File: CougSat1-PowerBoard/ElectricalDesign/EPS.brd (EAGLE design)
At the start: 90.4 x 95.8 mm, 414 parts, among them J1 Deployable 0, J11 CougSat Card, J2 PV1, J3 PV2, J5 SWD, J6 Umbilical, J7 PV0, J8 PV3, J9 Deployable 1, Q1 DMN53D0LDW, Q2 CSD25402Q3A, Q3 CSD25402Q3A, Q37 CSD25402Q3A, Q4 DMN2008LFU, Q5 CSD25402Q3A, Q6 DMN53D0LDW, Q8 DMN2008LFU, SW1 ESE24MH1, U1 TPS64200, U10 AD7689, U11 STM32L476RGT, U12 AD7689, U13 AD7291, U14 AD7291, U15 AD8515, U16 TPS64200, U17 AD8515, U18 INA199C1, U19 INA199C1, U2 AD7291, U20 BQ29700, U21 INA199C2, U22 INA199C1, U23 INA199C1, U24 INA199C1, U25 INA199C1, U26 TPS2115A, U27 TPS2115A, U28 TPS2115A, U29 TPS2115A, U3 AD7689, U30 TPS2115A, U31 TPS2115A, U32 TPS2115A, U33 TPS2115A, U34 TPS2115A, U35 TPS2115A, U36 TPS2115A, U37 TPS2115A, U38 TPS2115A, U39 TPS2115A, U4 TXS0102DQM, U40 TPS2115A, U41 TPS2115A, U42 TPS2115A, U43 TPS2115A, U44 TPS2115A, U45 TPS2115A, U46 TPS2115A, U47 TPS2115A, U48 TPS2115A, U49 TPS2115A, U5 TXS0102DQM, U50 TPS2115A, U51 AD8515, U52 TPS2115A, U53 TXS0102DQM, U54 TXS0102DQM, U55 TXS0102DQM, U6 BQ29700, U7 AD7291, U8 INA199C2, U9 AD7291, Y1 32.768kHz ±10ppm, Y2 8MHz ±10ppm

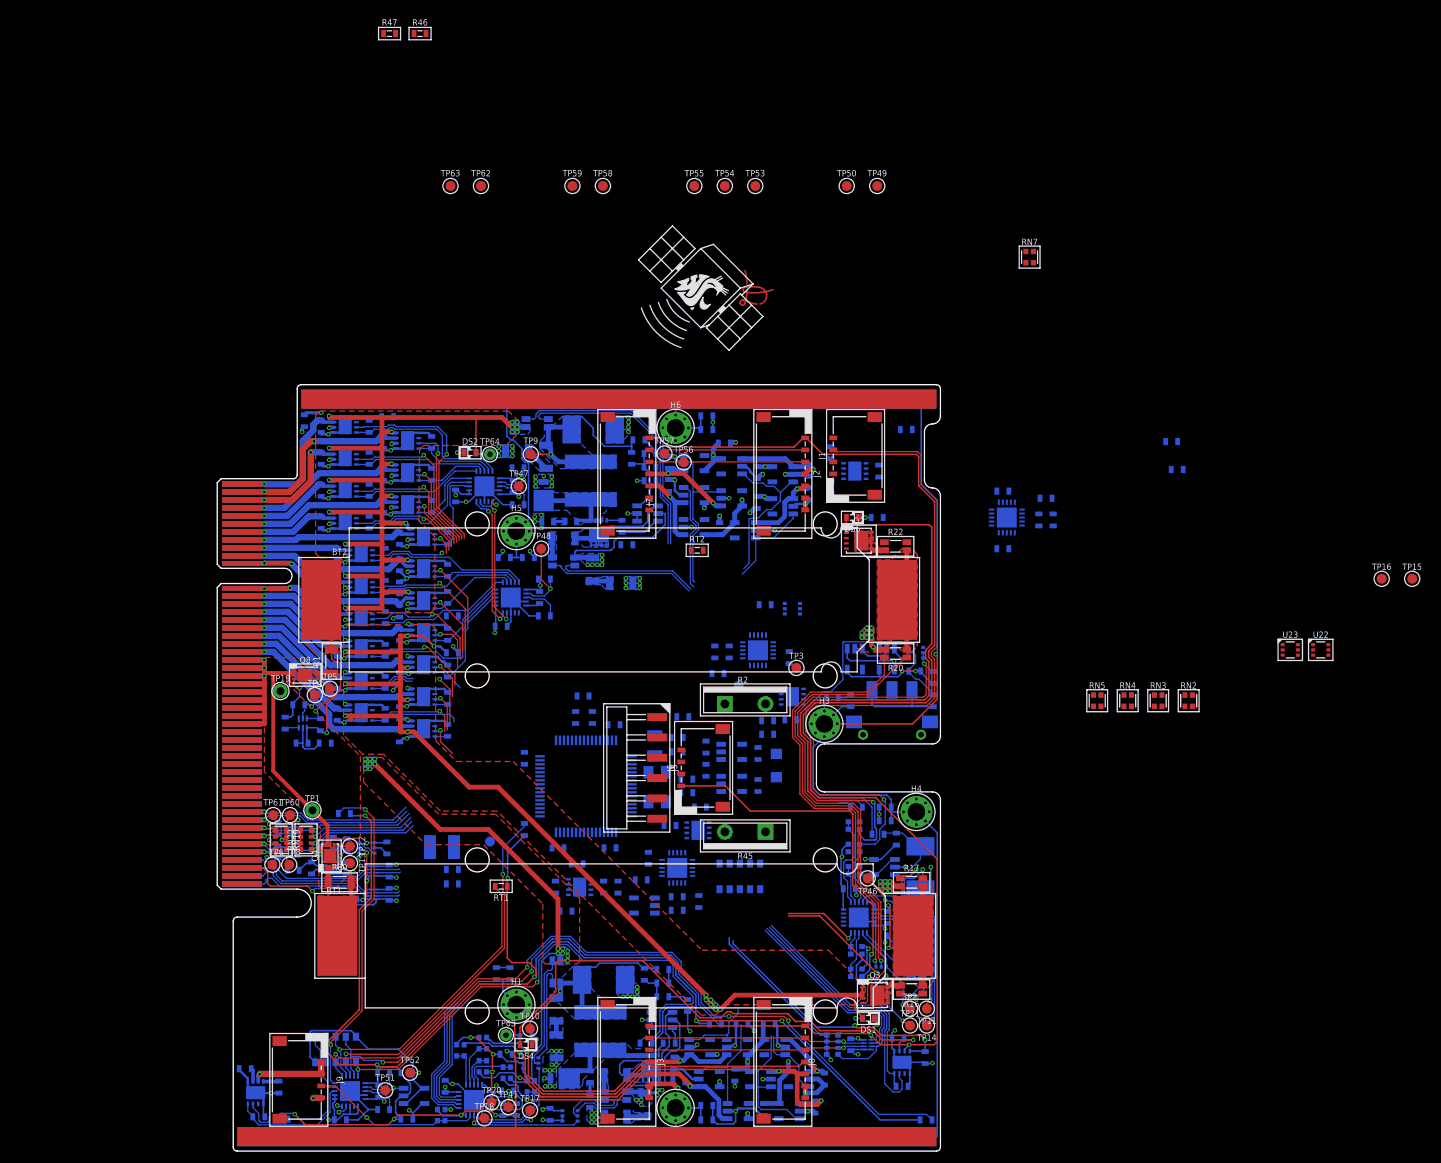
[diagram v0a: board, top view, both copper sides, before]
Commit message: Laid out temperature ADC and output switching control
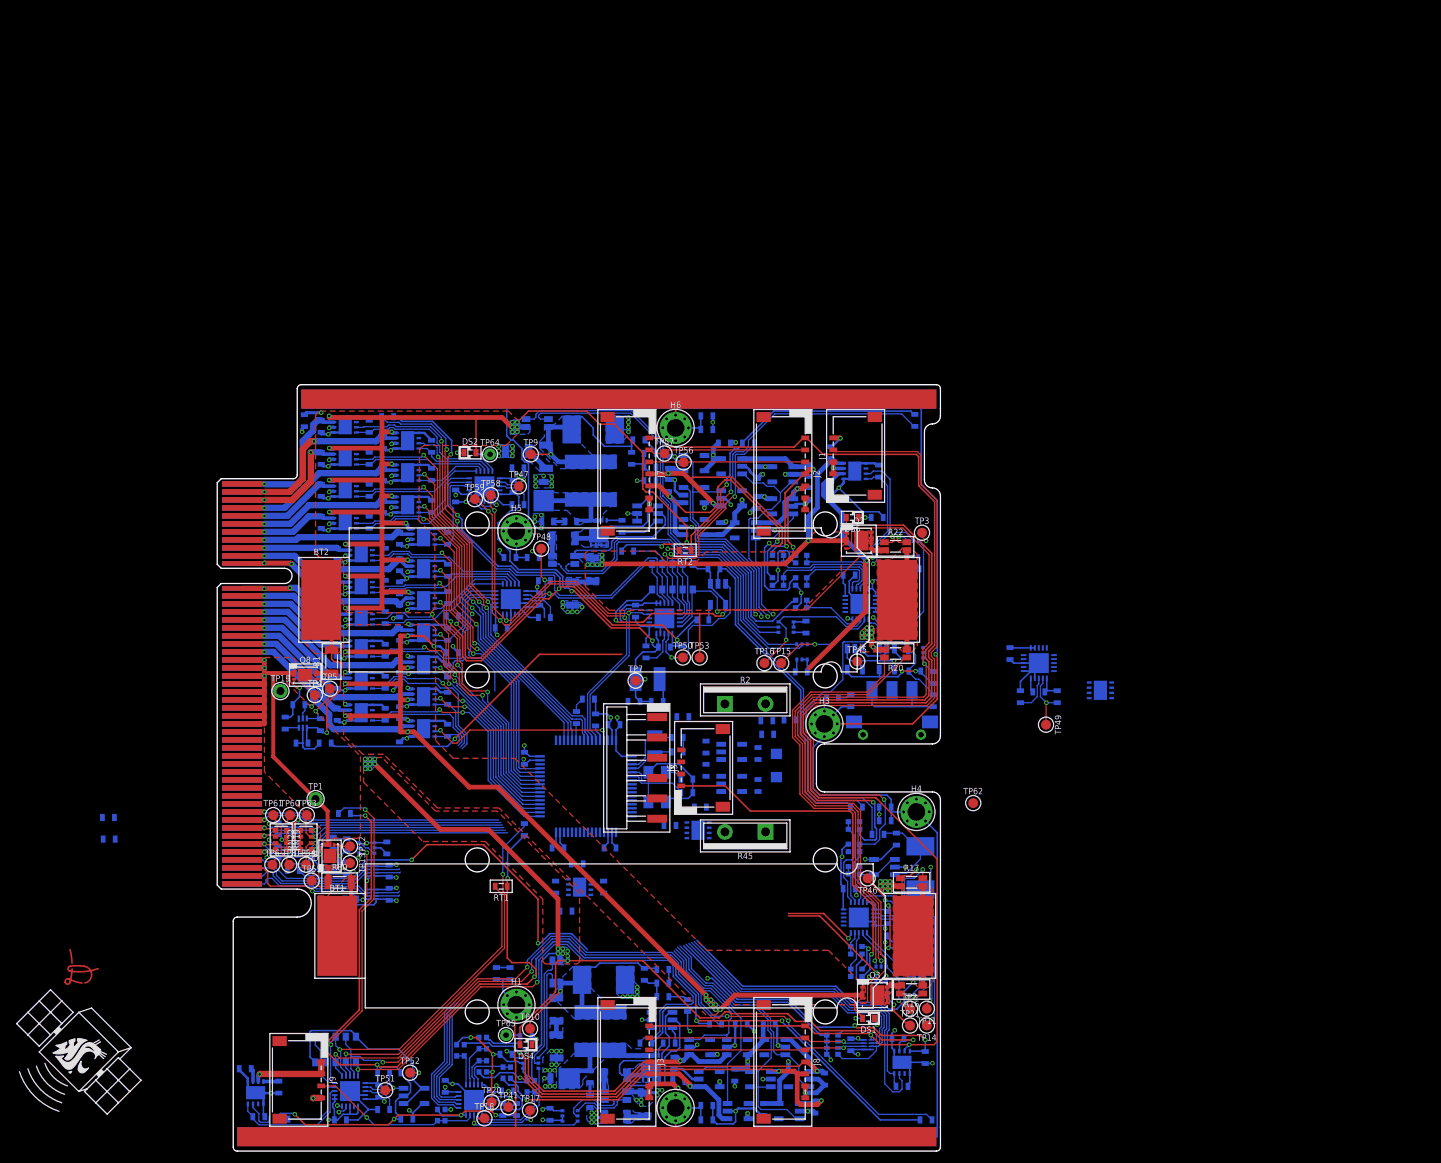
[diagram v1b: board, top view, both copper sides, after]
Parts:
- moved LOGO1 123.1 mm to (-17.3, -35.5)
- moved LOGO2 119.7 mm to (-16.9, -24.9)
- moved R46 107.9 mm to (-13.5, -8.90), flipped to the bottom, turned to 180 degrees
- moved R47 104.1 mm to (-13.6, -6.20), flipped to the bottom, turned to 180 degrees
- moved TP54 99.7 mm to (11.1, -12.1)
- moved TP55 99.1 mm to (11.8, -14.1)
- moved TP62 98.7 mm to (94.5, -4.40)
- moved TP63 80.7 mm to (11.2, -5.90)
- moved TP15 79.6 mm to (70.5, 13.1)
- moved TP16 77.9 mm to (68.4, 13.1)
- moved TP49 70.6 mm to (103.6, 5.40), turned to 270 degrees
- moved U22 64.8 mm to (73.1, 14.5), flipped to the bottom, turned to 90 degrees
- moved U23 63.1 mm to (71.1, 17.6), flipped to the bottom
- moved TP50 62.4 mm to (58.2, 13.8)
- moved TP53 59.3 mm to (60.3, 13.8)
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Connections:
- net !PC_3.3V-0: now also U11.57
- net !PC_3.3V-1: now also U11.56
- net !PC_3.3V-10: now also U11.41
- net !PC_3.3V-11: now also U11.39
- net !PC_3.3V-12: now also U11.40
- net !PC_3.3V-2: now also U11.53
- net !PC_3.3V-3: now also U11.52
- net !PC_3.3V-4: now also U11.51
- net !PC_3.3V-6: now also U11.45
- net !PC_3.3V-7: now also U11.44
- net !PC_3.3V-8: now also U11.43
- net !PC_3.3V-9: now also U11.42
- net !PC_BATT-0: now also U11.38
- net !PC_BATT-1: now also U11.37
- net !PC_BATT-2: now also U11.36
- net !PC_BATT-3: now also U11.35
- net !PC_BATT-4: now also U11.34
- net !PC_BATT-5: now also U11.33
- net !PC_BATT-6: now also U11.61
- net A: now also U7.2; no longer RN18.4, RN18.6, RN18.8, U9.1, U9.19, U9.2
- net ADC_3.3V-A: now also U10.9; no longer U10.7
- net ADC_EJECT_TIMER_BUF: no longer U10.8
- net ADC_VBATT-A: no longer U10.6
- net BUS_I2C_IRQ: no longer U11.57
- net BUS_I2C_SCL: now also U11.29; no longer U11.58
- net BUS_I2C_SDA: now also U11.30; no longer U11.59
- net DEPLOY_SENSE-0: no longer U10.9
- net I2C_SCL: now also U11.58; no longer U11.29
- net I2C_SDA: now also U11.59; no longer U11.30
- net I_3.3V_IN-A: now also U10.7
- net I_3.3V_OUT-A: now also U10.8
- net I_BATT_OUT-A: now also U10.6
- net I_DEPLOY-0: now also RN18.1, U9.5; no longer U7.2
- net TEMP-BATT-A: now also RN18.2, U9.3; no longer RN18.9, U9.18
- net TEMP-IN_SW-0: now also RN18.3, U9.1; no longer RN18.1, U9.5
- net TEMP-OUT_SW-0: now also RN18.6, U9.18; no longer RN18.3, U9.3
- net TEMP-OUT_SW-1: now also RN18.4, U9.19; no longer RN18.2, U9.4
- net TEMP-PCB-1: now also RN18.9, U9.4
- net TEMP-PCB-3: now also RN18.8, U9.2
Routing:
- net AGND: track 315.3 -> 534.0 mm, vias 21 -> 32
- net VIN_BATT-B: track 13.4 -> 100.1 mm, vias 0 -> 3
- net AVDD: track 115.6 -> 184.2 mm, vias 9 -> 12
- net 3.3V-A: track 145.7 -> 205.9 mm, vias 21 -> 22
- net TEMP-OUT_SW-1: track 0.00 -> 58.8 mm, vias 0 -> 2
- net DGND: track 133.5 -> 190.4 mm, vias 12 -> 14
- net I2C_SCL: track 48.3 -> 101.1 mm, vias 3 -> 4
- net TEMP-PCB-3: track 0.00 -> 52.3 mm, vias 0 -> 2
- net TEMP-PCB-1: track 4.56 -> 54.7 mm
- net I2C_SDA: track 50.1 -> 99.9 mm, vias 3 -> 4
- net VBATT-A: track 169.7 -> 217.6 mm, vias 14 -> 15
- net I_DEPLOY-0: track 0.00 -> 46.1 mm, vias 0 -> 2
- net VIN_BATT-A: track 13.6 -> 54.9 mm, vias 0 -> 1
- net TEMP-OUT_SW-0: track 0.00 -> 39.9 mm, vias 0 -> 2
- net PGND: track 886.4 -> 923.7 mm, vias 115 -> 118
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- added copper zone on layer 1, net VBATT-A

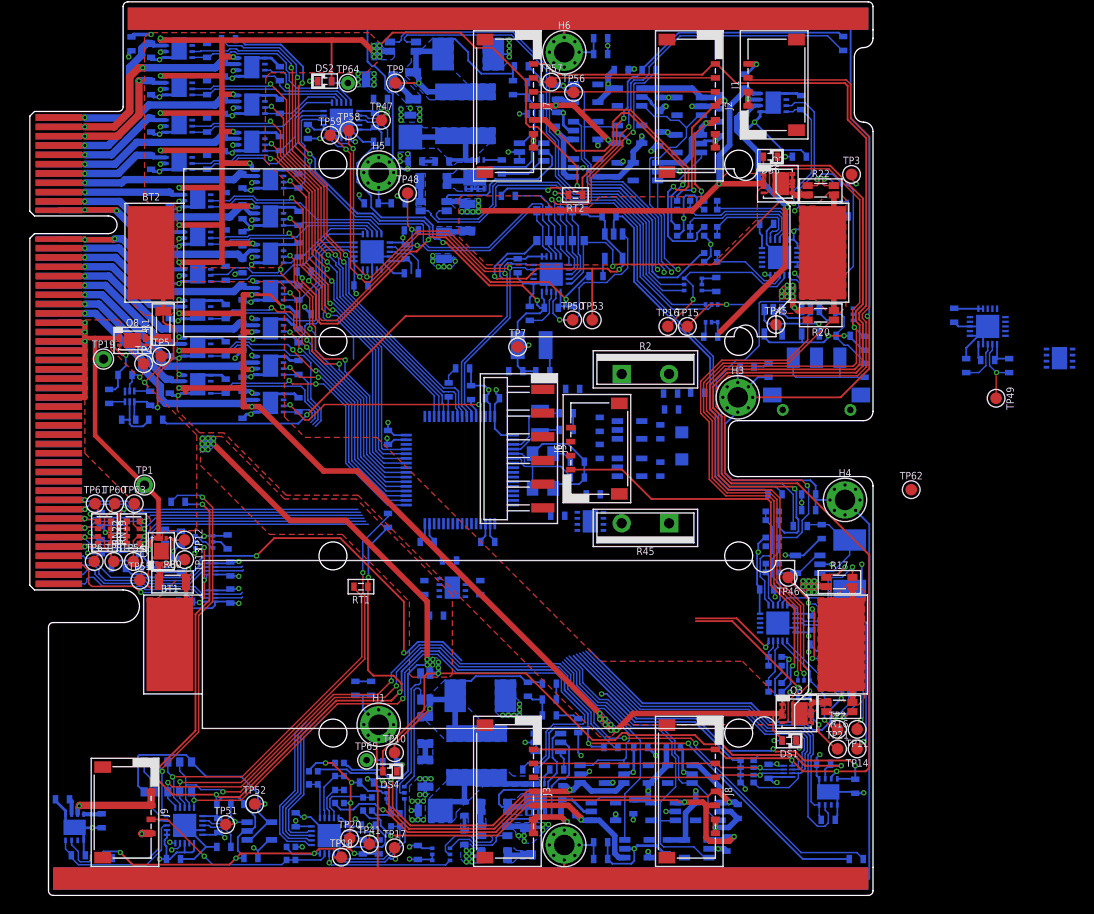
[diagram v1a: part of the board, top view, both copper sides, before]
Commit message: Laid out JTAG, BH-0, and remaining ADC
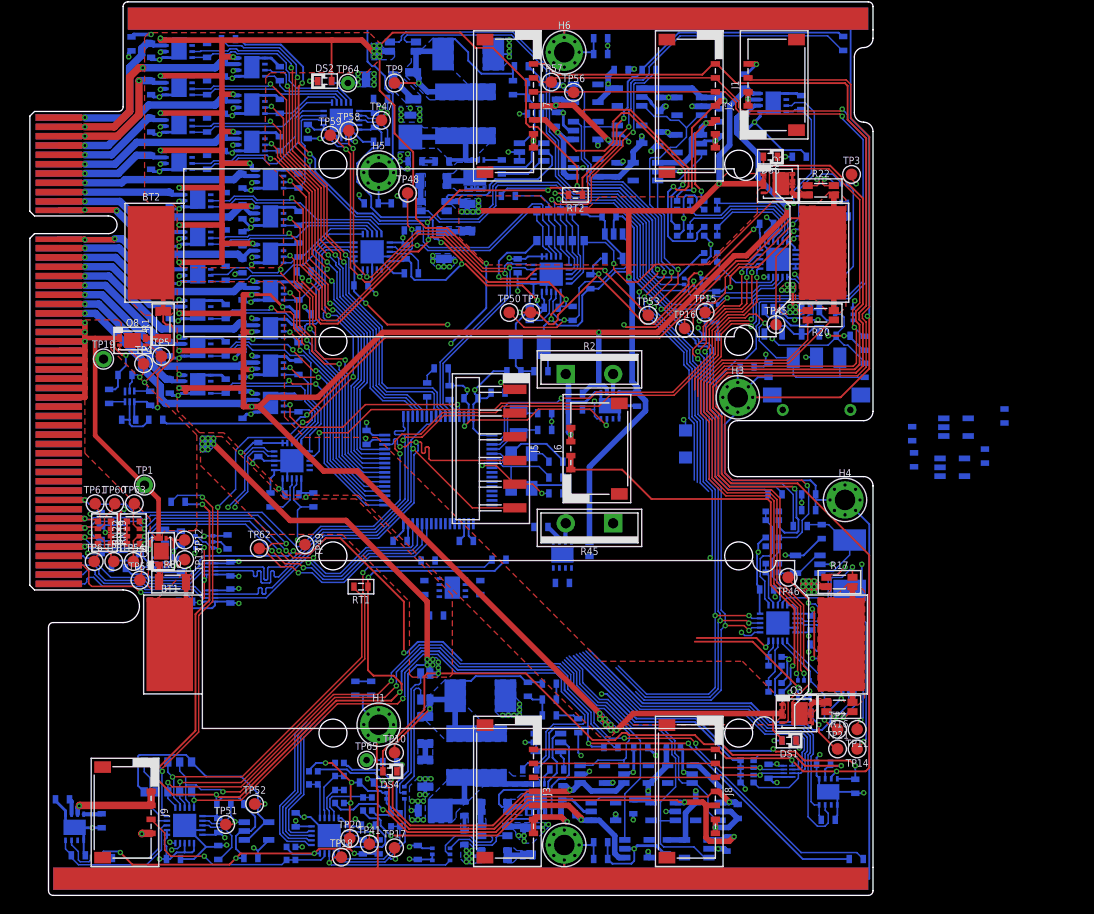
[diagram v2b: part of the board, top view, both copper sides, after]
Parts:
- added C72, C73: 100nF 10%, CougsInSpace-Capacitors:1608
- moved C156 76.0 mm to (25.8, -5.50)
- moved C157 76.0 mm to (30.4, -5.50)
- moved C158 76.0 mm to (24.5, -0.10)
- moved C159 76.0 mm to (28.1, -4.90)
- moved U7 76.0 mm to (28.1, -1.30)
- moved TP49 75.7 mm to (29.5, -10.3)
- moved TP62 70.2 mm to (24.6, -10.7)
- moved U47 48.5 mm to (62.2, 4.60), turned to 90 degrees
- moved C60 36.9 mm to (104.5, 3.50)
- moved D25 35.0 mm to (99.3, 2.30)
- moved C61 34.8 mm to (102.4, -0.80)
- moved D26 34.6 mm to (98.9, -2.00)
- moved C59 33.7 mm to (94.8, -1.20)
- moved R114 33.5 mm to (94.6, 1.60)
- moved R65 13.2 mm to (58.5, 4.20)
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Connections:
- removed net A: U7.2, U7.3
- removed net CTRL_!RESET: J11.A41, J11.B41
- new net N$2: U7.3
- new net N$3: U7.4
- new net N$4: U7.5
- net !PC_BH-0: now also U11.62
- net ADC_SEL-1: now also U11.2
- net BUS_I2C_IRQ: now also U11.28
- net CTRL_SYNC: now also U11.27
- net I_BATT-3: now also U7.1; no longer U7.18
- net I_BATT-4: now also U7.20; no longer U7.19
- net I_BATT-5: now also U7.19; no longer U7.20
- net I_BATT-6: now also U7.18; no longer U7.1
- net I_BH-0: now also U7.2; no longer U7.4
- net I_BH-1: no longer U7.5
- net PGND: now also C72.2, C73.2
- net VBATT-A: now also C72.1
- net VBATT-B: now also C73.1
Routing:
- net DGND: track 190.4 -> 333.1 mm, vias 14 -> 20
- net 3.3V: track 185.5 -> 320.4 mm, vias 17 -> 22
- net AGND: track 534.0 -> 608.4 mm, vias 32 -> 39
- net PWR_CTRL_SW: track 47.0 -> 115.5 mm, vias 1 -> 3
- net SPI_MISO: track 16.4 -> 84.9 mm, vias 0 -> 4
- net SPI_SCK: track 15.8 -> 84.0 mm, vias 0 -> 4
- net SPI_MOSI: track 16.5 -> 81.0 mm, vias 0 -> 4
- net PV_I2C_SDA: track 47.7 -> 109.9 mm, vias 1 -> 3
- net VBATT-B: track 200.5 -> 261.3 mm, vias 23 -> 24
- net PV_I2C_SCL: track 47.3 -> 107.0 mm, vias 1 -> 3
- net PGND: track 923.7 -> 979.6 mm, vias 118 -> 122
- net AVDD: track 184.2 -> 237.4 mm, vias 12 -> 18
- net JTAG_TMS: track 2.99 -> 50.5 mm, vias 0 -> 2
- net JTAG_TDO: track 3.03 -> 50.5 mm, vias 0 -> 1
- net JTAG_TCK: track 2.99 -> 50.2 mm, vias 0 -> 1
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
